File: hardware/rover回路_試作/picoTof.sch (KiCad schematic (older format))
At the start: 7 parts

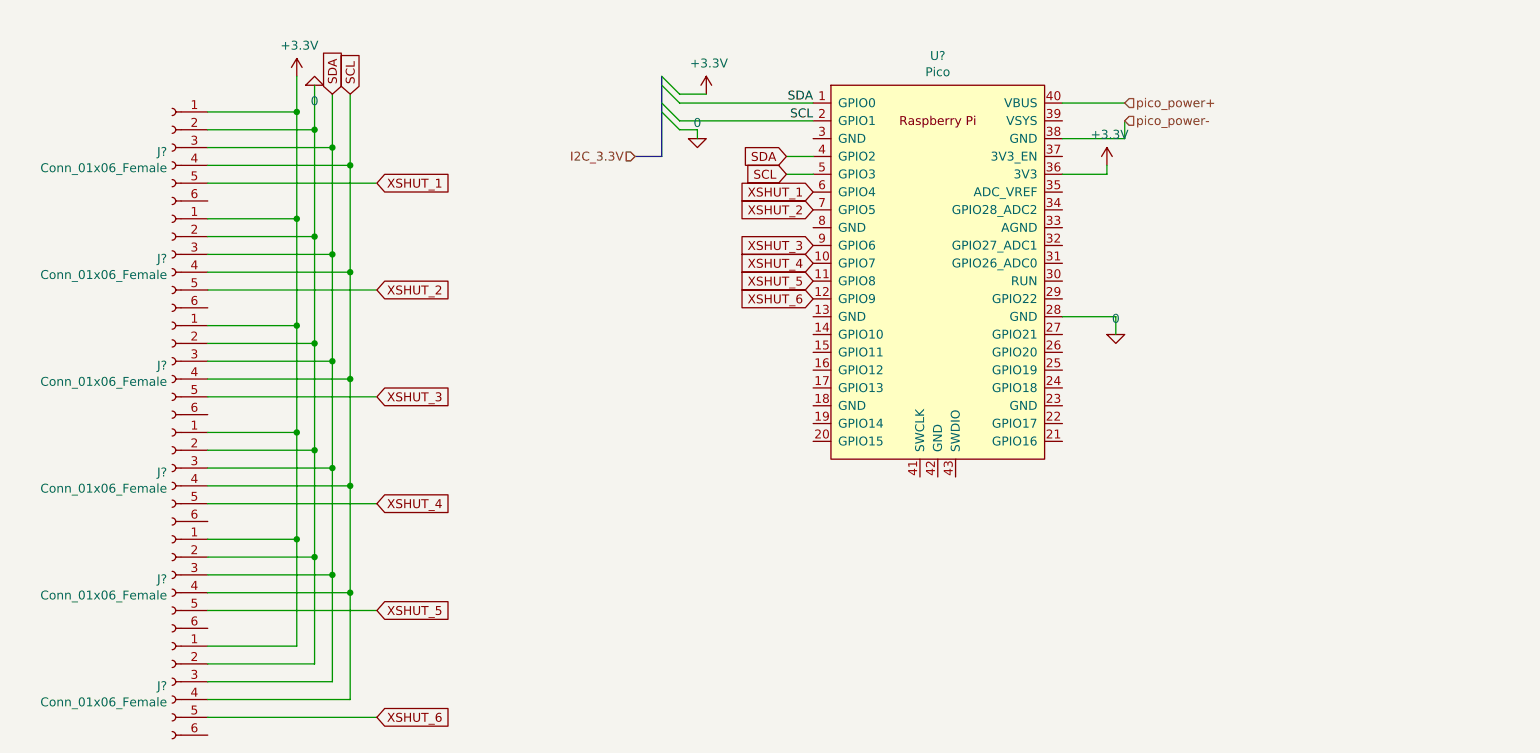
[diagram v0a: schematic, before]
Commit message: rover回路最終版v1.0 降圧回路に関してのみ未記載
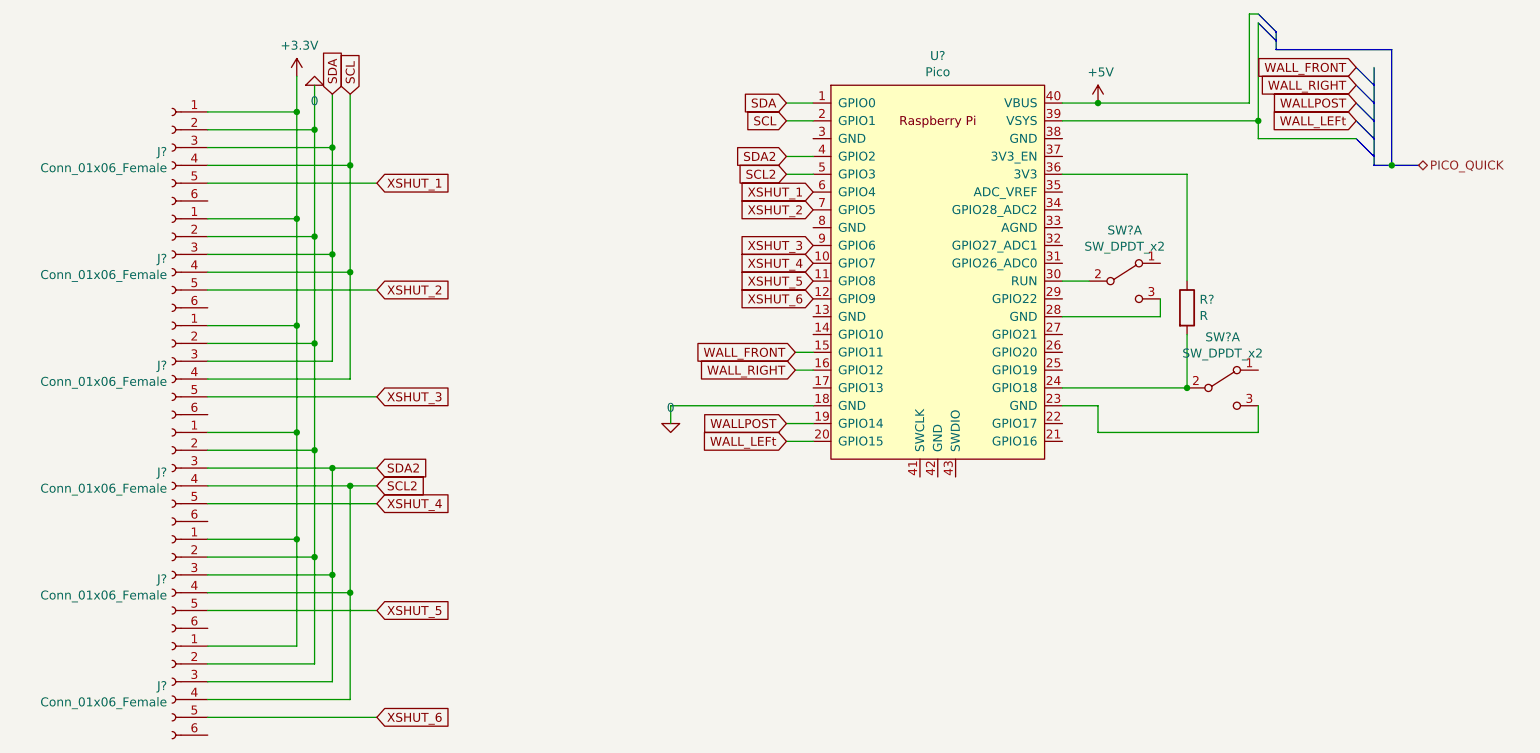
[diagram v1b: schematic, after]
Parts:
- added R?: R, symbol Device:R
- added SW? (x2): SW_DPDT_x2, symbol Switch:SW_DPDT_x2
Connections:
- net labels added: +5V, PICO_QUICK, SCL2, SDA2, WALLPOST, WALL_FRONT, WALL_LEFt, WALL_RIGHT
- net labels removed: I2C_3.3V, pico_power+, pico_power-
- wire segments 68 -> 83
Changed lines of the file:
@@
 $Descr A4 11693 8268
 encoding utf-8
-Sheet 2 7
+Sheet 2 8
 Title ""
 Date ""
@@
 	1    0    0    -1
 $EndComp
-Text HLabel 8600 2400 2    50   Input ~ 0
-pico_power+
-Text HLabel 8600 2500 2    50   Input ~ 0
-pico_power-
-Wire Wire Line
-	8600 2500 8600 2600
-Wire Wire Line
-	8600 2600 8250 2600
-Wire Wire Line
-	8250 2400 8600 2400
-$Comp
-L power:+3.3V #PWR?
-U 1 1 617DF518
-P 8500 2750
-F 0 "#PWR?" H 8500 2600 50  0001 C CNN
-F 1 "+3.3V" H 8515 2923 50  0000 C CNN
-F 2 "" H 8500 2750 50  0001 C CNN
-F 3 "" H 8500 2750 50  0001 C CNN
-	1    8500 2750
-	1    0    0    -1
-$EndComp
+Wire Wire Line
+	8250 2400 8450 2400
 $Comp
 L pspice:0 #GND?
 U 1 1 617DF7FF
-P 8550 3700
-F 0 "#GND?" H 8550 3600 50  0001 C CNN
-F 1 "0" H 8550 3789 50  0000 C CNN
-F 2 "" H 8550 3700 50  0001 C CNN
-F 3 "~" H 8550 3700 50  0001 C CNN
-	1    8550 3700
-	1    0    0    -1
-$EndComp
-Wire Wire Line
-	8250 2800 8500 2800
-Wire Wire Line
-	8500 2800 8500 2750
-Wire Wire Line
-	8250 3600 8550 3600
-Wire Wire Line
-	8550 3600 8550 3700
-Text Label 6850 2400 2    50   ~ 0
-SDA
-Text Label 6850 2500 2    50   ~ 0
+P 6050 4200
+F 0 "#GND?" H 6050 4100 50  0001 C CNN
+F 1 "0" H 6050 4289 50  0000 C CNN
+F 2 "" H 6050 4200 50  0001 C CNN
+F 3 "~" H 6050 4200 50  0001 C CNN
+	1    6050 4200
+	-1   0    0    -1
+$EndComp
+Wire Wire Line
+	6050 4100 6050 4200
+Text GLabel 6700 2500 0    50   Input ~ 0
 SCL
-Text GLabel 6700 2800 0    50   Input ~ 0
-SCL
-Text GLabel 6700 2700 0    50   Input ~ 0
+Text GLabel 6700 2400 0    50   Input ~ 0
 SDA
 $Comp
@@
 	-1   0    0    -1
 $EndComp
-Text GLabel 4250 2350 1    50   Input ~ 0
-SCL
 Text GLabel 4150 2350 1    50   Input ~ 0
 SDA
@@
 Wire Wire Line
 	3450 4650 4400 4650
-Connection ~ 3950 3650
-Wire Wire Line
-	3950 3650 3950 4250
-Connection ~ 3950 4250
-Connection ~ 4050 3750
-Wire Wire Line
-	4050 3750 4050 4350
-Connection ~ 4050 4350
-Connection ~ 4150 3850
-Wire Wire Line
-	4150 3850 4150 4450
-Connection ~ 4150 4450
-Connection ~ 4250 3950
-Wire Wire Line
-	4250 3950 4250 4550
-Connection ~ 4250 4550
-Wire Wire Line
-	6850 2700 6700 2700
-Wire Wire Line
-	6700 2800 6850 2800
+Wire Wire Line
+	6850 2400 6700 2400
+Wire Wire Line
+	6700 2500 6850 2500
 Text GLabel 4400 2850 2    50   Input ~ 0
 XSHUT_1
@@
 XSHUT_4
 $Comp
-L pspice:0 #GND?
-U 1 1 6180EDD5
-P 6200 2600
-F 0 "#GND?" H 6200 2500 50  0001 C CNN
-F 1 "0" H 6200 2689 50  0000 C CNN
-F 2 "" H 6200 2600 50  0001 C CNN
-F 3 "~" H 6200 2600 50  0001 C CNN
-	1    6200 2600
-	1    0    0    -1
-$EndComp
-$Comp
-L power:+3.3V #PWR?
-U 1 1 61811F2F
-P 6250 2350
-F 0 "#PWR?" H 6250 2200 50  0001 C CNN
-F 1 "+3.3V" H 6265 2523 50  0000 C CNN
-F 2 "" H 6250 2350 50  0001 C CNN
-F 3 "" H 6250 2350 50  0001 C CNN
-	1    6250 2350
-	1    0    0    -1
-$EndComp
-Wire Wire Line
-	6100 2350 6250 2350
-Wire Wire Line
-	6100 2400 6850 2400
-Wire Wire Line
-	6100 2500 6850 2500
-Wire Wire Line
-	6100 2550 6200 2550
-Wire Wire Line
-	6200 2550 6200 2600
-Entry Wire Line
-	6000 2250 6100 2350
-Entry Wire Line
-	6000 2300 6100 2400
-Entry Wire Line
-	6000 2400 6100 2500
-Entry Wire Line
-	6000 2450 6100 2550
-Wire Bus Line
-	6000 2700 5850 2700
-Text HLabel 5850 2700 0    50   Input ~ 0
-I2C_3.3V
-$Comp
 L Connector:Conn_01x06_Female J?
 U 1 1 6165B6FE
@@
 Text GLabel 6850 3500 0    50   Input ~ 0
 XSHUT_6
-Wire Bus Line
-	6000 2250 6000 2700
+$Comp
+L Switch:SW_DPDT_x2 SW?
+U 1 1 6170B581
+P 8600 3400
+F 0 "SW?" H 8600 3685 50  0000 C CNN
+F 1 "SW_DPDT_x2" H 8600 3594 50  0000 C CNN
+F 2 "" H 8600 3400 50  0001 C CNN
+F 3 "~" H 8600 3400 50  0001 C CNN
+	1    8600 3400
+	1    0    0    -1
+$EndComp
+Wire Wire Line
+	8250 3400 8400 3400
+Wire Wire Line
+	8800 3600 8250 3600
+$Comp
+L power:+5V #PWR?
+U 1 1 61714813
+P 8450 2400
+F 0 "#PWR?" H 8450 2250 50  0001 C CNN
+F 1 "+5V" H 8465 2573 50  0000 C CNN
+F 2 "" H 8450 2400 50  0001 C CNN
+F 3 "" H 8450 2400 50  0001 C CNN
+	1    8450 2400
+	1    0    0    -1
+$EndComp
+Connection ~ 8450 2400
+Wire Wire Line
+	8800 3500 8800 3600
+$Comp
+L Switch:SW_DPDT_x2 SW?
+U 1 1 6176D1FA
+P 9150 4000
+F 0 "SW?" H 9150 4285 50  0000 C CNN
+F 1 "SW_DPDT_x2" H 9150 4194 50  0000 C CNN
+F 2 "" H 9150 4000 50  0001 C CNN
+F 3 "~" H 9150 4000 50  0001 C CNN
+	1    9150 4000
+	1    0    0    -1
+$EndComp
+Wire Wire Line
+	8250 4100 8450 4100
+Wire Wire Line
+	8450 4100 8450 4250
+Wire Wire Line
+	8450 4250 9350 4250
+Wire Wire Line
+	9350 4100 9350 4250
+Wire Wire Line
+	8250 4000 8950 4000
+$Comp
+L Device:R R?
+U 1 1 61783364
+P 8950 3550
+F 0 "R?" H 9020 3596 50  0000 L CNN
+F 1 "R" H 9020 3505 50  0000 L CNN
+F 2 "" V 8880 3550 50  0001 C CNN
+F 3 "~" H 8950 3550 50  0001 C CNN
+	1    8950 3550
+	1    0    0    -1
+$EndComp
+Wire Wire Line
+	8950 2800 8950 3400
+Wire Wire Line
+	8950 3700 8950 4000
+Connection ~ 8950 4000
+Connection ~ 4050 4350
+Connection ~ 4050 3750
+Wire Wire Line
+	4050 3750 4050 4350
+Connection ~ 3950 4250
+Connection ~ 3950 3650
+Wire Wire Line
+	3950 3650 3950 4250
+Text GLabel 4250 2350 1    50   Input ~ 0
+SCL
+Text GLabel 4400 4450 2    50   Input ~ 0
+SDA2
+Text GLabel 4400 4550 2    50   Input ~ 0
+SCL2
+Wire Wire Line
+	4150 4450 4400 4450
+Connection ~ 4150 4450
+Wire Wire Line
+	4250 4550 4400 4550
+Connection ~ 4250 4550
+Text GLabel 6700 2700 0    50   Input ~ 0
+SDA2
+Text GLabel 6700 2800 0    50   Input ~ 0
+SCL2
+Wire Wire Line
+	6700 2700 6850 2700
+Wire Wire Line
+	6850 2800 6700 2800
+Wire Wire Line
+	8950 2800 8250 2800
+Text GLabel 6750 3800 0    50   Input ~ 0
+WALL_FRONT
+Text GLabel 6750 3900 0    50   Input ~ 0
+WALL_RIGHT
+Text GLabel 6700 4200 0    50   Input ~ 0
+WALLPOST
+Text GLabel 6700 4300 0    50   Input ~ 0
+WALL_LEFt
+Wire Wire Line
+	6050 4100 6850 4100
+Wire Wire Line
+	6850 4200 6700 4200
+Wire Wire Line
+	6850 4300 6700 4300
+Wire Wire Line
+	6750 3900 6850 3900
+Wire Wire Line
+	6850 3800 6750 3800
+Text GLabel 9900 2200 0    50   Input ~ 0
+WALL_FRONT
+Text GLabel 9900 2300 0    50   Input ~ 0
+WALL_RIGHT
+Text GLabel 9900 2400 0    50   Input ~ 0
+WALLPOST
+Text GLabel 9900 2500 0    50   Input ~ 0
+WALL_LEFt
+Wire Wire Line
+	8250 2500 9350 2500
+Wire Wire Line
+	9350 2500 9350 2600
+Wire Wire Line
+	9350 2600 9900 2600
+Wire Wire Line
+	8450 2400 9300 2400
+Entry Bus Bus
+	9900 2200 10000 2300
+Entry Bus Bus
+	9900 2300 10000 2400
+Entry Bus Bus
+	9900 2400 10000 2500
+Entry Bus Bus
+	9900 2500 10000 2600
+Entry Bus Bus
+	9900 2600 10000 2700
+Text HLabel 10250 2750 2    50   BiDi ~ 0
+PICO_QUICK
+Wire Bus Line
+	10000 2750 10100 2750
+Connection ~ 9350 2500
+Entry Bus Bus
+	9350 1950 9450 2050
+Entry Bus Bus
+	9350 1900 9450 2000
+Wire Wire Line
+	9350 1950 9350 2500
+Wire Wire Line
+	9300 1900 9350 1900
+Wire Wire Line
+	9300 1900 9300 2400
+Wire Bus Line
+	9450 2100 10100 2100
+Wire Bus Line
+	10100 2100 10100 2750
+Wire Bus Line
+	9450 2000 9450 2100
+Wire Bus Line
+	10000 2200 10000 2750
+Connection ~ 10100 2750
+Wire Bus Line
+	10100 2750 10250 2750
 $EndSCHEMATC

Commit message: DCDC回路図追加
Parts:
- U?: symbol Rpi_Pico:Pico -> power-rescue:Pico-Rpi_Pico
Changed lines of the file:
@@
 $EndDescr
 $Comp
-L Rpi_Pico:Pico U?
+L power-rescue:Pico-Rpi_Pico U?
 U 1 1 617DE19D
 P 7550 3350
